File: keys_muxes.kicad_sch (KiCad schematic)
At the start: 30 parts, among them SW1 SW_Push, SW10 SW_Push, SW11 SW_Push, SW12 SW_Push, SW13 SW_Push, SW14 SW_Push, SW15 SW_Push, SW16 SW_Push, SW17 SW_Push, SW18 SW_Push, SW19 SW_Push, SW2 SW_Push, SW20 SW_Push, SW21 SW_Push, SW22 SW_Push, SW23 SW_Push, SW24 SW_Push, SW25 SW_Push, SW26 SW_Push, SW27 SW_Push, SW3 SW_Push, SW4 SW_Push, SW5 SW_Push, SW6 SW_Push, SW7 SW_Push, SW8 SW_Push, SW9 SW_Push, U2 74HC4051, U3 74HC4051, U4 74HC4051

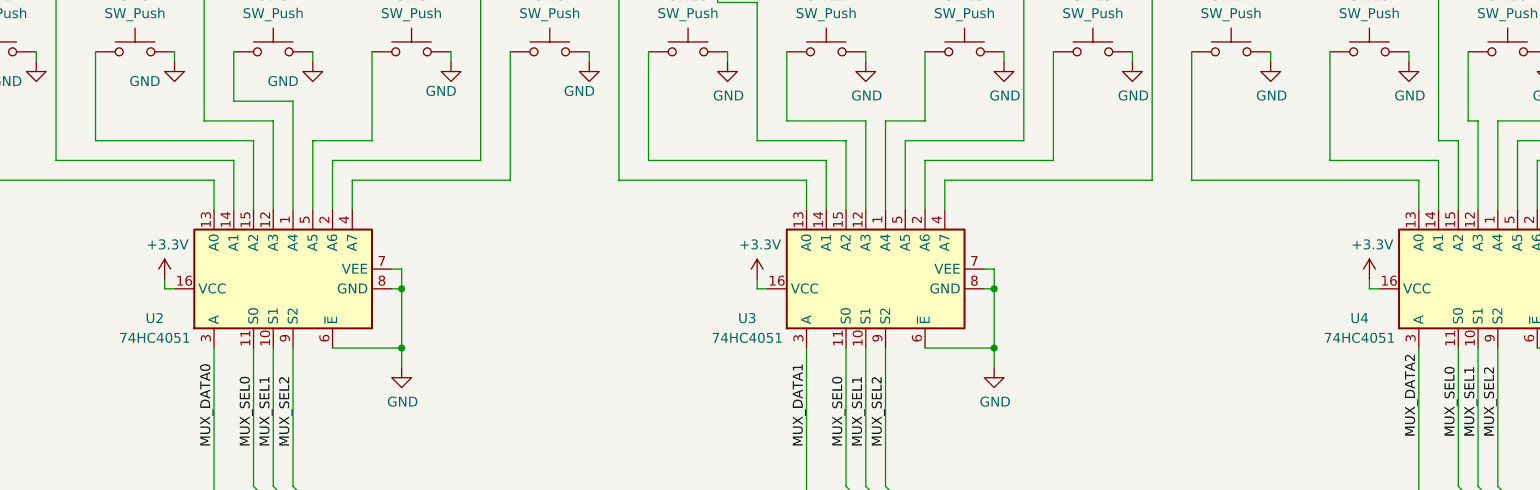
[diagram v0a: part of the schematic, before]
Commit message: update to Kicad v9
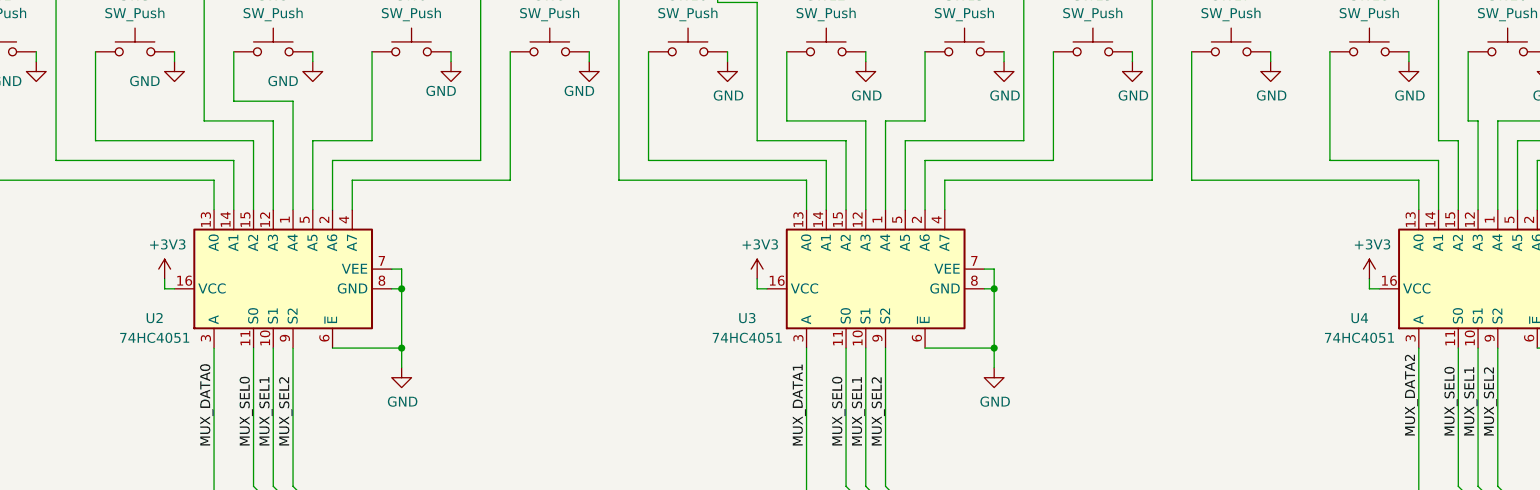
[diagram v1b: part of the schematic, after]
